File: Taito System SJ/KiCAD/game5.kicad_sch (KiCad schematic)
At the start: 11 parts, among them U32 7496, U33 74LS02, U35 74LS02, U36 7496, U53 74LS04

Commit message: Update before transfer
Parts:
- removed U32, U36: 7496, symbol 74xx_IEEE:7496
- added U10, U11, U12, U20, U21, U22, U32, U36: 74LS96, symbol ag74xx:74LS96
- added U13, U19, U23, U9: 74LS253, symbol jt74:74LS253
- added U34: 74LS259, symbol jt74:74LS259
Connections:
- net GND: now also U10.12 (GND), U11.12 (GND), U12.12 (GND), U20.12 (GND), U21.12 (GND), U22.12 (GND), U32.12 (GND), U36.12 (GND)
- net GNDPWR: now also U10.1 (CK), U10.9 (SER), U11.1 (CK), U11.9 (SER), U12.1 (CK), U12.9 (SER), U20.1 (CK), U20.9 (SER), U21.1 (CK), U21.9 (SER), U22.1 (CK), U22.9 (SER), U32.1 (CK), U32.9 (SER), U34.14 (E), U34.15 (Clr), U36.1 (CK), U36.9 (SER), U9.13 (I3b)
- net HTCLR: now also U10.16 (~{R}), U11.16 (~{R}), U12.16 (~{R}), U20.16 (~{R}), U22.16 (~{R}), U32.16 (~{R}), U36.16 (~{R})
- net S12: now also U19.13 (I3b), U36.11 (Q3)
- net S13: now also U13.3 (I3a), U32.15 (Q0)
- net S23: now also U13.13 (I3b), U32.14 (Q1)
- net VCC: now also U10.5 (VCC), U11.5 (VCC), U12.5 (VCC), U13.16 (VCC), U19.16 (VCC), U20.5 (VCC), U21.5 (VCC), U22.5 (VCC), U23.16 (VCC), U32.5 (VCC), U34.16 (VCC), U36.5 (VCC), U9.16 (VCC)
- net at C?.1, U35.1: now also U36.2 (P0)
- net at C?.1, U33.13: now also U32.2 (P0)
- net at C?.1, U33.4: now also U32.3 (P1)
- net at C?.1, U35.13: now also U36.3 (P1)
- net at C?.1, U35.4: now also U36.4 (P2)
- net at C?.1, U35.10: now also U36.6 (P3)
- net at U53.6: now also U32.8 (PE), U36.8 (PE)
- new net 16HM: U34.1 (A0)
- new net 32HM: U34.2 (A1)
- new net 64HM: U34.3 (A2)
- new net A0: U13.14 (A0), U19.14 (A0), U23.14 (A0), U9.14 (A0)
- new net A1: U13.2 (A1), U19.2 (A1), U23.2 (A1), U9.2 (A1)
- new net EXT_DATA_D0: U23.7 (Za)
- new net EXT_DATA_D1: U23.9 (Zb)
- new net EXT_DATA_D2: U19.7 (Za)
- new net EXT_DATA_D3: U19.9 (Zb)
- new net EXT_DATA_D4: U13.7 (Za)
- new net EXT_DATA_D5: U13.9 (Zb)
- new net EXT_DATA_D6: U9.7 (Za)
- new net EXT_DATA_D7: U9.9 (Zb)
- new net H0: U20.15 (Q0), U23.6 (I0a)
- new net H1: U20.14 (Q1), U23.10 (I0b)
- new net H10: U19.5 (I1a), U21.13 (Q2)
- new net H11: U19.11 (I1b), U21.11 (Q3)
- new net H12: U11.15 (Q0), U13.5 (I1a)
- new net H13: U11.14 (Q1), U13.11 (I1b)
- new net H14: U11.13 (Q2), U9.5 (I1a)
- new net H15: U11.11 (Q3), U9.11 (I1b)
- new net H16: U22.15 (Q0), U23.4 (I2a)
- new net H17: U22.14 (Q1), U23.12 (I2b)
- new net H18: U19.4 (I2a), U22.13 (Q2)
- new net H19: U19.12 (I2b), U22.11 (Q3)
- new net H2: U19.6 (I0a), U20.13 (Q2)
- new net H20: U12.15 (Q0), U13.4 (I2a)
- new net H21: U12.14 (Q1), U13.12 (I2b)
- new net H22: U12.13 (Q2), U9.4 (I2a)
- new net H23: U12.11 (Q3), U9.12 (I2b)
- new net H3: U19.10 (I0b), U20.11 (Q3)
- new net H4: U10.15 (Q0), U13.6 (I0a)
- new net H5: U10.14 (Q1), U13.10 (I0b)
- new net H6: U10.13 (Q2), U9.6 (I0a)
- new net H7: U10.11 (Q3), U9.10 (I0b)
- new net H8: U21.15 (Q0), U23.5 (I1a)
- new net H9: U21.14 (Q1), U23.11 (I1b)
- new net HD0: U20.2 (P0), U21.2 (P0), U22.2 (P0), U34.4 (Q0)
- new net HD1: U20.3 (P1), U21.3 (P1), U22.3 (P1), U34.5 (Q1)
- new net HD2: U20.4 (P2), U21.4 (P2), U22.4 (P2), U34.6 (Q2)
- new net HD3: U20.6 (P3), U21.6 (P3), U22.6 (P3), U34.7 (Q3)
- new net HD4: U10.2 (P0), U11.2 (P0), U12.2 (P0), U34.9 (Q4)
- new net HD5: U10.3 (P1), U11.3 (P1), U12.3 (P1), U34.10 (Q5)
- new net HD6: U10.4 (P2), U11.4 (P2), U12.4 (P2), U34.11 (Q6)
- new net HD7: U10.6 (P3), U11.6 (P3), U12.6 (P3), U34.12 (Q7)
- new net HITON: U34.13 (D)
- new net HLP0: U10.8 (PE), U20.8 (PE)
- new net HLP1: U11.8 (PE), U21.8 (PE)
- new net HLP2: U12.8 (PE), U22.8 (PE)
- new net HTRRQ: U13.1 (OEa), U13.15 (OEb), U19.1 (OEa), U19.15 (OEb), U23.1 (OEa), U23.15 (OEb), U9.1 (OEa), U9.15 (OEb)
- new net OB1: U23.3 (I3a), U36.15 (Q0)
- new net OB2: U23.13 (I3b), U36.14 (Q1)
- new net OB3: U19.3 (I3a), U36.13 (Q2)
- new net VSS: U13.8 (VSS), U19.8 (VSS), U23.8 (VSS), U34.8 (VSS), U9.8 (VSS)
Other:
- moved on the sheet: U33B, U33D, U35A, U35B, U35C, U35D, U53C

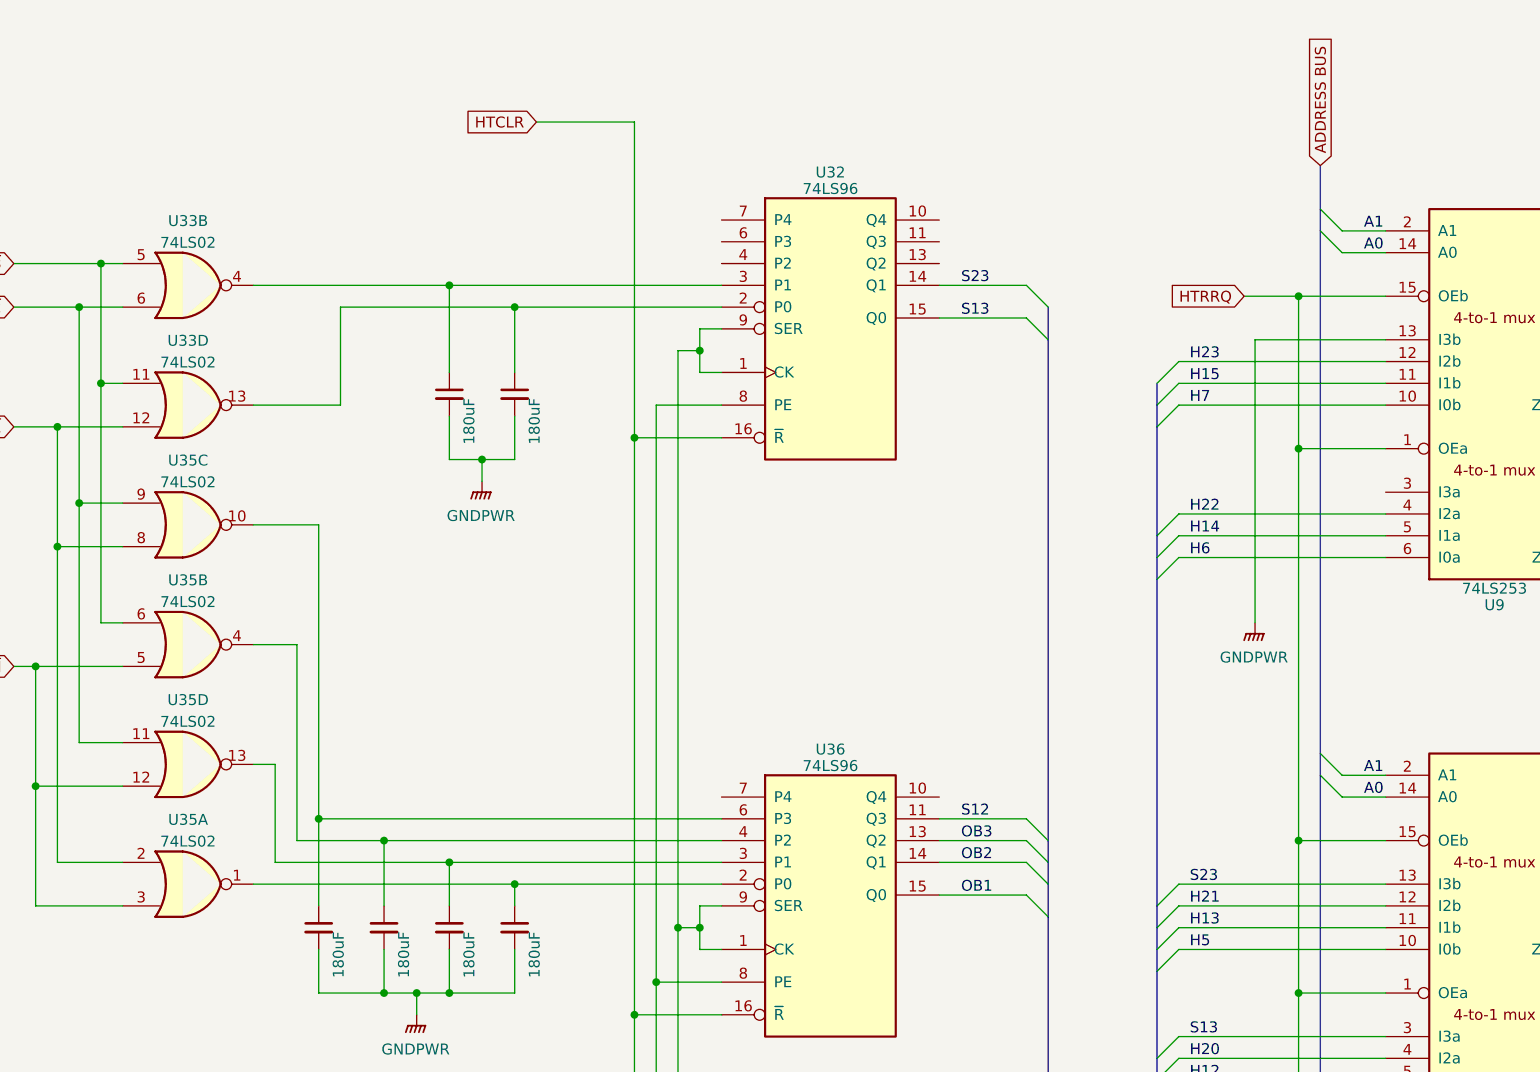
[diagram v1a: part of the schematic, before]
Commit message: Added MCU to Taito SJ Schematics
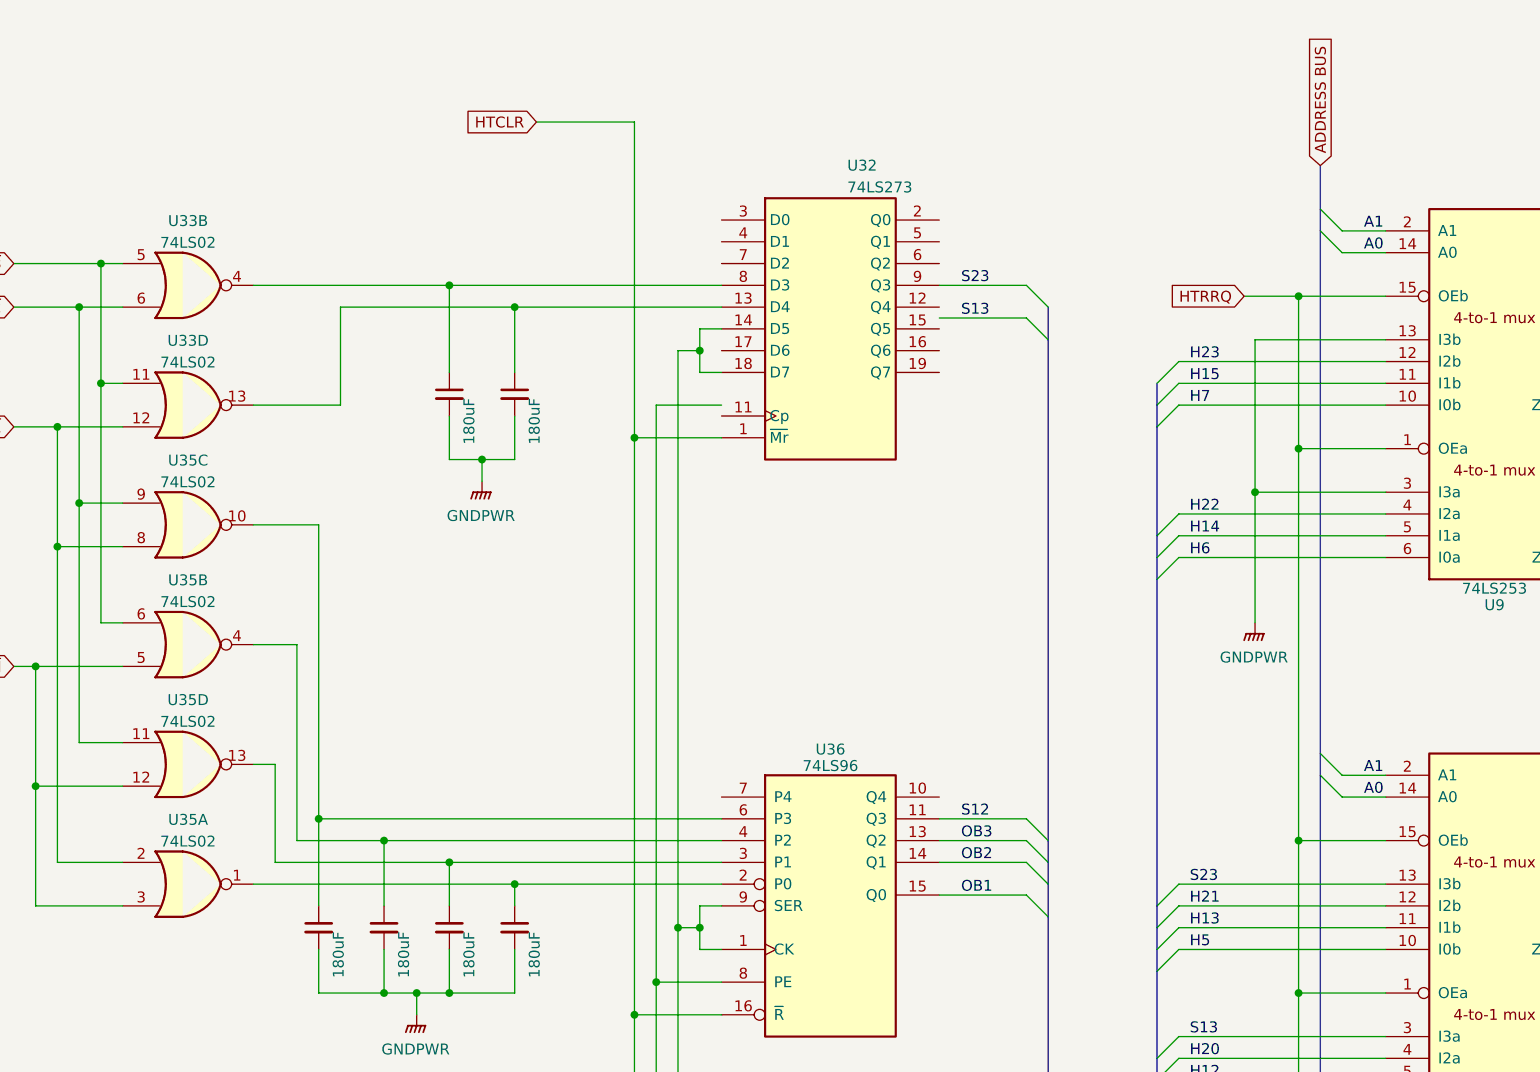
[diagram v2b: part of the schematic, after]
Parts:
- U32: value 74LS96 -> 74LS273
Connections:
- net GND: now also U32.10 (GND); no longer U32.12 (GND)
- net GNDPWR: now also U32.14 (D5), U32.18 (D7), U9.3 (I3a); no longer U32.1 (CK), U32.9 (SER)
- net HTCLR: now also U32.1 (~{Mr}); no longer U32.16 (~{R})
- net S13: no longer U32.15 (Q0)
- net S23: now also U32.9 (Q3); no longer U32.14 (Q1)
- net VCC: now also U32.20 (VCC); no longer U32.5 (VCC)
- net at C?.1, U33.13: now also U32.13 (D4); no longer U32.2 (P0)
- net at C?.1, U33.4: now also U32.8 (D3); no longer U32.3 (P1)
- net at U36.8 (PE), U53.6: no longer U32.8 (PE)
